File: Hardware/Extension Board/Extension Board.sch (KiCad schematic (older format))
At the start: 34 parts, among them J1 CNX_LED, J10 MODE, J11 TUNING, J12 I2C, J13 I2C, J14 SPI, J15 SD, J16 TFT, J2 CNX_LED, J3 CNX_LED, J4 CNX_LED, J5 SPARE, J6 ARDUINO_DIGITAL, J7 ARDUINO_COMMS, J8 ARDUINO_ANALOG, J9 NEXT_AGAIN, U1 74HC14

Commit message: update shematics
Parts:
- removed J15: SD, Connector_JST:JST_XH_B4B-XH-AM_1x04_P2.50mm_Vertical, symbol Connector_Generic:Conn_01x04
- removed J16: TFT, Connector_JST:JST_XH_B8B-XH-AM_1x08_P2.50mm_Vertical, symbol Connector_Generic:Conn_01x08
- added J15, J5: CNX_LED, Connector_JST:JST_XH_B2B-XH-A_1x02_P2.50mm_Vertical, symbol Connector_Generic:Conn_01x02
- added R11, R12: 200, Resistor_THT:R_Axial_DIN0207_L6.3mm_D2.5mm_P10.16mm_Horizontal, symbol Device:R
- added TP3: TestPoint_Flag, TestPoint:TestPoint_Loop_D2.54mm_Drill1.5mm_Beaded, symbol Connector:TestPoint_Flag
- added U2: LM7806_TO220, Package_TO_SOT_THT:TO-220-3_Vertical, symbol Regulator_Linear:LM7806_TO220
- added U3: LM7812_TO220, Package_TO_SOT_THT:TO-220-3_Vertical, symbol Regulator_Linear:LM7812_TO220
- renumbered J5 to J16
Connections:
- net D17 is gone; now on net SDA: J7.5 (Pin_5)
- net A12: now also J8.5 (Pin_5); no longer J8.4 (Pin_4)
- net A14: now also J8.7 (Pin_7); no longer J8.2 (Pin_2)
- net D18: now also J7.3 (Pin_3); no longer J7.4 (Pin_4)
- net D19: now also J7.4 (Pin_4); no longer J7.3 (Pin_3)
- net GND: no longer TP2.1
- net SCL: now also J7.6 (Pin_6); no longer J7.1 (Pin_1)
- net SDA: no longer J7.2 (Pin_2)
- net VCC: now also J15.1 (Pin_1), J5.1 (Pin_1); no longer TP1.1
- net at J1.2 (Pin_2): now also R11.1; no longer R1.1
- net at J16.2 (Pin_2): now also R12.1; no longer R5.1
- net D35: now reaches J6.15 (Pin_15)
- net D35: now also R11.2
- net D37: now reaches J6.17 (Pin_17)
- net D37: now also R12.2
- net TFT_LED: no longer names the net of R9.1
- net TFT_LED: no longer R10.1
- new net: J15.2 (Pin_2), R1.1
- new net: J5.2 (Pin_2), R5.1
- no-connect marks 25 -> 24
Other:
- note added: "A15 ... ... A8"
- note added: "ALIMENTATION"
- note added: "D21 ... ... D16"
- note removed: "SPI OLED DISPLAY"
- moved on the sheet: J1, J16, TP1, TP2

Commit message: Ajout FootPrint Library MesModules
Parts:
- removed J1, J15, J2, J3, J4, J5: CNX_LED, Connector_JST:JST_XH_B2B-XH-A_1x02_P2.50mm_Vertical, symbol Connector_Generic:Conn_01x02
- removed R4: 200, Resistor_THT:R_Axial_DIN0207_L6.3mm_D2.5mm_P10.16mm_Horizontal, symbol Device:R
- removed R9: 50k, Resistor_THT:R_Axial_DIN0207_L6.3mm_D2.5mm_P10.16mm_Horizontal, symbol Device:R
- added C3: 100uF, Capacitor_THT:CP_Axial_L18.0mm_D8.0mm_P25.00mm_Horizontal, symbol Device:CP
- added C4: 2200uF, Capacitor_THT:CP_Axial_L30.0mm_D18.0mm_P35.00mm_Horizontal, symbol Device:CP
- added C5, C6: 10uF, Capacitor_THT:CP_Radial_D5.0mm_P2.50mm, symbol Device:CP
- added HS1: Heatsink, MesModules:HeatSink_TO-220, symbol Mechanical:Heatsink
- added J10: CNX ON_OFF, Connector_JST:JST_XH_B2B-XH-A_1x02_P2.50mm_Vertical, symbol Connector_Generic:Conn_01x02
- added J13: CNX_LAMPS, MesModules:Bloc_de_jonction_CI-MPT_2.54mm_01x02, symbol Connector:Screw_Terminal_01x02
- added J14: CNX_6V, TerminalBlock_Phoenix:TerminalBlock_Phoenix_MKDS-1,5-2-5.08_1x02_P5.08mm_Horizontal, symbol Connector:Screw_Terminal_01x02
- added J15: CNX_12V, TerminalBlock_Phoenix:TerminalBlock_Phoenix_MKDS-1,5-2-5.08_1x02_P5.08mm_Horizontal, symbol Connector:Screw_Terminal_01x02
- added J6: CNX LEDS, symbol Connector_Generic:Conn_02x05_Odd_Even
- added J9: CNX POWER, TerminalBlock_Phoenix:TerminalBlock_Phoenix_MKDS-1,5-2-5.08_1x02_P5.08mm_Horizontal, symbol Connector:Screw_Terminal_01x02
- added JP1: Jumper, Connector_PinHeader_2.54mm:PinHeader_1x02_P2.54mm_Vertical, symbol Device:Jumper_NC_Small
- added JP2: Jumper, Connector_PinHeader_2.54mm:PinHeader_1x02_P2.54mm_Vertical, symbol Device:Jumper_NO_Small
- added R11: 3k3, Resistor_THT:R_Axial_DIN0207_L6.3mm_D2.5mm_P10.16mm_Horizontal, symbol Device:R
- added TP4: TestPoint 12V, TestPoint:TestPoint_Loop_D2.54mm_Drill1.5mm_Beaded, symbol Connector:TestPoint_Flag
- J11: value TUNING -> CNX TUNE
- J4: renamed from J14; value SPI -> CNX SPI
- J5: renamed from J10; value MODE -> CNX MODE
- J7: renamed from J16; value SPARE -> CNX SPARE; footprint Connector_JST:JST_XH_B3B-XH-A_1x03_P2.50mm_Vertical -> Connector_JST:JST_XH_B3B-XH-AM_1x03_P2.50mm_Vertical
- R10: value 90k -> 3k3
- R7, R8: value 4.7k -> 3k3
- R9: renamed from R6; value A CALCULER -> 3M; footprint Resistor_THT:R_Axial_DIN0411_L9.9mm_D3.6mm_P20.32mm_Horizontal -> (none)
- TP1: value TestPoint_Flag -> TestPoint GND
- TP2: value TestPoint_Flag -> TestPoint VDD
- TP3: value TestPoint_Flag -> TestPoint 6V
- renumbered J6 to J1, J13 to J16, J7 to J2, J8 to J3, J9 to J8, R5 to R1, R11 to R2, R1 to R3, R2 to R4, R3 to R5, R12 to R6
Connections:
- net A12: now also JP1.1, JP2.1; no longer J11.2 (Pin_2)
- net GND: now also TP1.1, U2.2 (GND), U3.2 (GND), C3.2, C4.2, C5.2, C6.2, J13.2 (Pin_2), J14.2 (Pin_2), J15.2 (Pin_2), J9.1 (Pin_1), JP2.2
- net SCL: now also R11.2
- net SDA: now also R10.2
- net VCC: now also R10.1, TP3.1, U2.3 (VO), C5.1, J13.1 (Pin_1), J14.1 (Pin_1), J6.10 (Pin_10), J6.2 (Pin_2), J6.4 (Pin_4), J6.6 (Pin_6), J6.8 (Pin_8), R11.1; no longer R10.2
- net at R5.1: now also J6.9 (Pin_9)
- net at R4.1: now also J6.7 (Pin_7)
- net at R2.1: now also J6.3 (Pin_3)
- net VDD: now reaches TP2.1
- net VDD: now also U2.1 (VI), U3.1 (VI), C3.1, C4.1, J10.2 (Pin_2)
- net at R3.1: now also J6.5 (Pin_5)
- net at R1.1: now also J6.1 (Pin_1)
- net +12V: now reaches U3.3 (VO)
- net +12V: now also C6.1, J15.1 (Pin_1), TP4.1
- new net: J10.1 (Pin_1), J9.2 (Pin_2)
- new net C1: J11.2 (Pin_2), JP1.2
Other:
- note added: "Adaptation pour Push Buttons \n(avec IRQ)"
- note added: "Adaptation pour \nRotary Button"
- note added: "Ampli 7W/12V:\n→600mA"
- note added: "I2C bus"
- note added: "Spare connectors"
- note added: "verifier s'il faut connecter à la masse"
- note removed: "Adaptation pour Push Buttons (avec IRQ)"
- note removed: "Adaptation pour Rotary Button"
- note removed: "SPI and I2C bus"
- moved on the sheet: C1, C2, J11, J12, J16, J2, J4, J5, J7, J8, R1, R2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

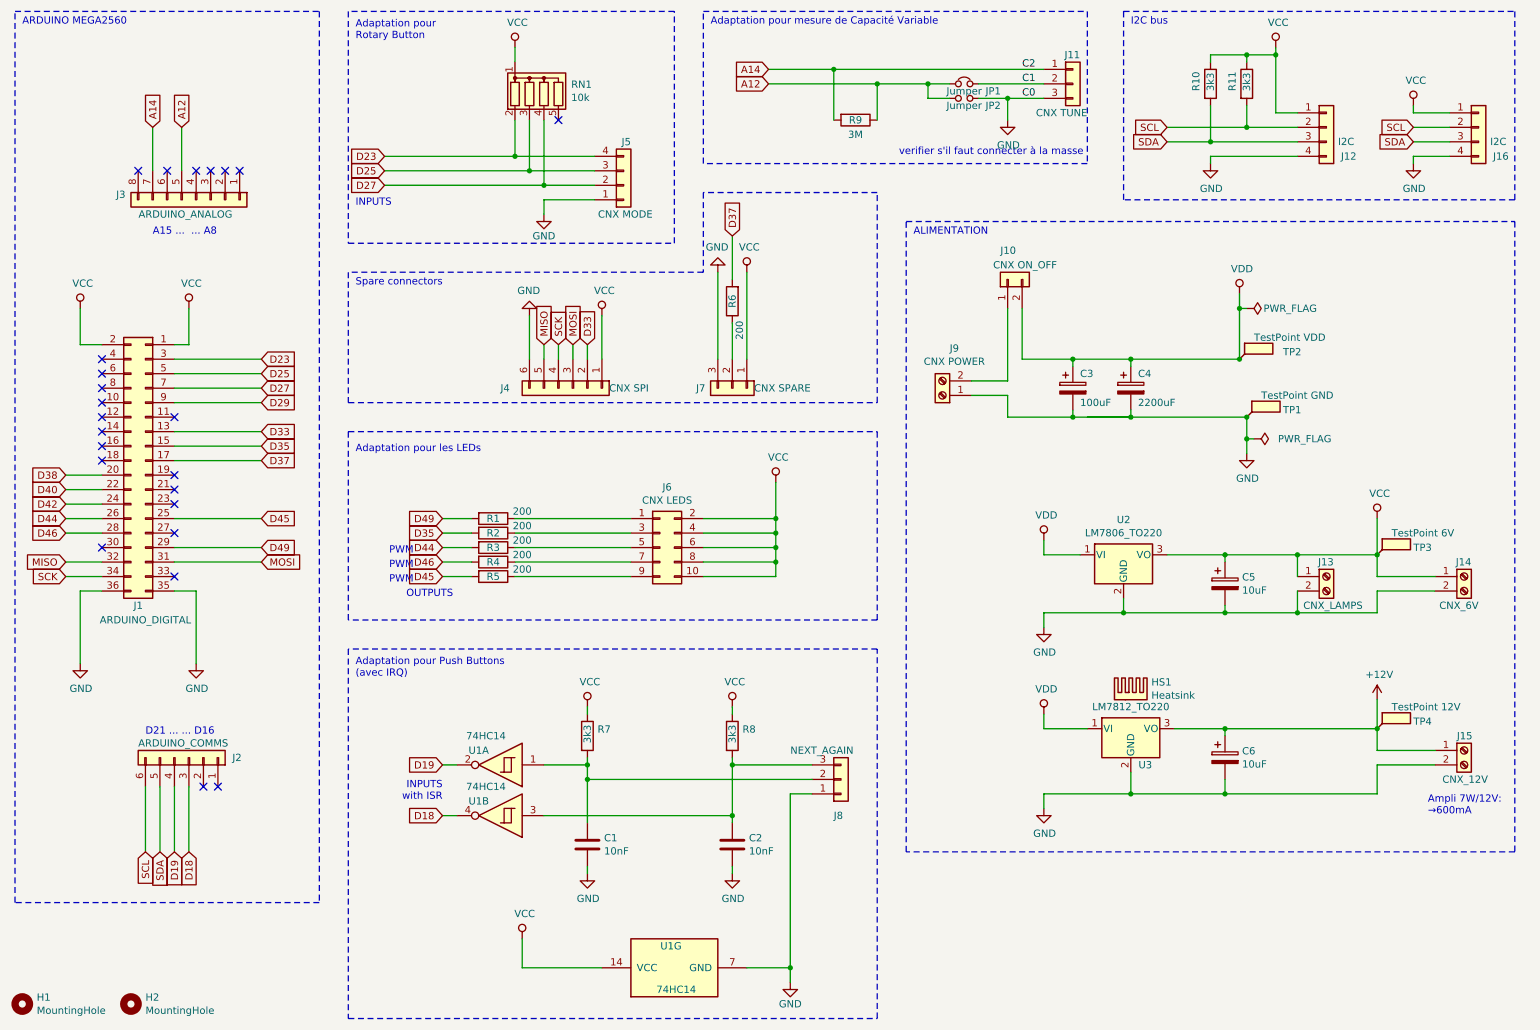
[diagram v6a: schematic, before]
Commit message: Ajout du connecteur HE10 10P dans la Library KiCad
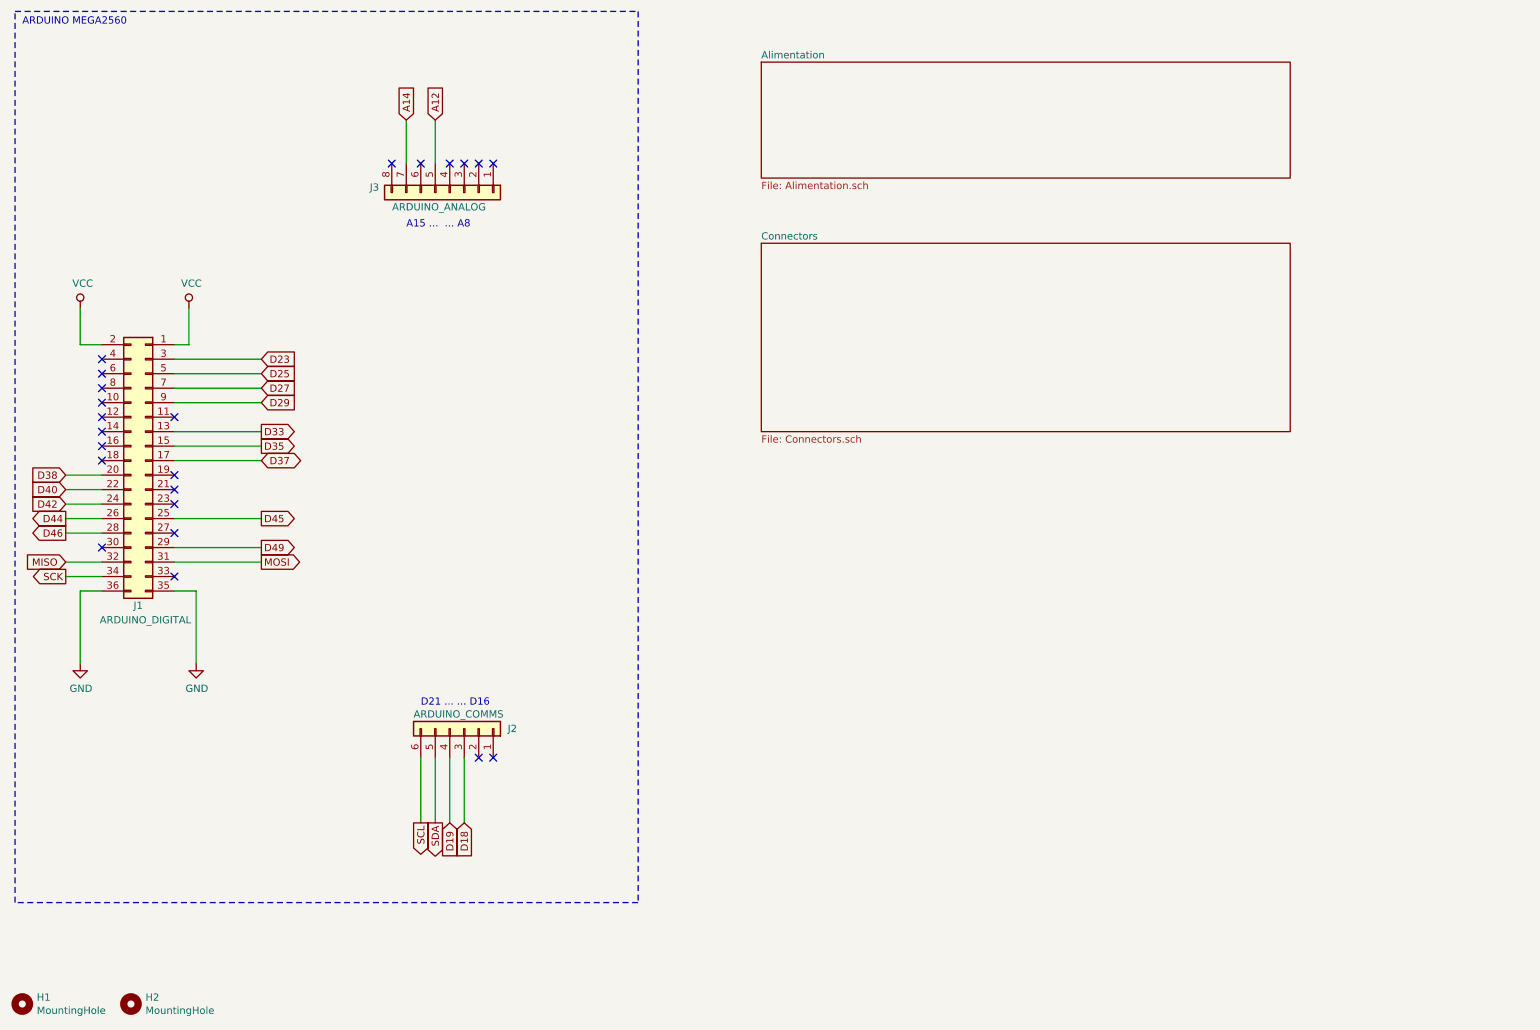
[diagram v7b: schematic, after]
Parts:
- removed C1, C2: 10nF, Capacitor_THT:C_Rect_L7.2mm_W2.5mm_P5.00mm_FKS2_FKP2_MKS2_MKP2, symbol Device:C
- removed C3: 100uF, Capacitor_THT:CP_Axial_L18.0mm_D8.0mm_P25.00mm_Horizontal, symbol Device:CP
- removed C4: 2200uF, Capacitor_THT:CP_Axial_L30.0mm_D18.0mm_P35.00mm_Horizontal, symbol Device:CP
- removed C5, C6: 10uF, Capacitor_THT:CP_Radial_D5.0mm_P2.50mm, symbol Device:CP
- removed HS1: Heatsink, MesModules:HeatSink_TO-220, symbol Mechanical:Heatsink
- removed J10: CNX ON_OFF, Connector_JST:JST_XH_B2B-XH-A_1x02_P2.50mm_Vertical, symbol Connector_Generic:Conn_01x02
- removed J11: CNX TUNE, Connector_JST:JST_XH_B3B-XH-A_1x03_P2.50mm_Vertical, symbol Connector_Generic:Conn_01x03
- removed J12, J16: I2C, Connector_JST:JST_XH_B4B-XH-A_1x04_P2.50mm_Vertical, symbol Connector_Generic:Conn_01x04
- removed J13: CNX_LAMPS, MesModules:Bloc_de_jonction_CI-MPT_2.54mm_01x02, symbol Connector:Screw_Terminal_01x02
- removed J14: CNX_6V, TerminalBlock_Phoenix:TerminalBlock_Phoenix_MKDS-1,5-2-5.08_1x02_P5.08mm_Horizontal, symbol Connector:Screw_Terminal_01x02
- removed J15: CNX_12V, TerminalBlock_Phoenix:TerminalBlock_Phoenix_MKDS-1,5-2-5.08_1x02_P5.08mm_Horizontal, symbol Connector:Screw_Terminal_01x02
- removed J4: CNX SPI, Connector_JST:JST_XH_B6B-XH-AM_1x06_P2.50mm_Vertical, symbol Connector_Generic:Conn_01x06
- removed J5: CNX MODE, Connector_JST:JST_XH_B4B-XH-A_1x04_P2.50mm_Vertical, symbol Connector_Generic:Conn_01x04
- removed J6: CNX LEDS, symbol Connector_Generic:Conn_02x05_Odd_Even
- removed J7: CNX SPARE, Connector_JST:JST_XH_B3B-XH-AM_1x03_P2.50mm_Vertical, symbol Connector_Generic:Conn_01x03
- removed J8: NEXT_AGAIN, Connector_JST:JST_XH_B3B-XH-A_1x03_P2.50mm_Vertical, symbol Connector_Generic:Conn_01x03
- removed J9: CNX POWER, TerminalBlock_Phoenix:TerminalBlock_Phoenix_MKDS-1,5-2-5.08_1x02_P5.08mm_Horizontal, symbol Connector:Screw_Terminal_01x02
- removed JP1: Jumper, Connector_PinHeader_2.54mm:PinHeader_1x02_P2.54mm_Vertical, symbol Device:Jumper_NC_Small
- removed JP2: Jumper, Connector_PinHeader_2.54mm:PinHeader_1x02_P2.54mm_Vertical, symbol Device:Jumper_NO_Small
- removed R1, R2, R3, R4, R5, R6: 200, Resistor_THT:R_Axial_DIN0207_L6.3mm_D2.5mm_P10.16mm_Horizontal, symbol Device:R
- removed R10, R11, R7, R8: 3k3, Resistor_THT:R_Axial_DIN0207_L6.3mm_D2.5mm_P10.16mm_Horizontal, symbol Device:R
- removed R9: 3M, symbol Device:R
- removed RN1: 10k, Resistor_THT:R_Array_SIP5, symbol Device:R_Network04
- removed TP1: TestPoint GND, TestPoint:TestPoint_Loop_D2.54mm_Drill1.5mm_Beaded, symbol Connector:TestPoint_Flag
- removed TP2: TestPoint VDD, TestPoint:TestPoint_Loop_D2.54mm_Drill1.5mm_Beaded, symbol Connector:TestPoint_Flag
- removed TP3: TestPoint 6V, TestPoint:TestPoint_Loop_D2.54mm_Drill1.5mm_Beaded, symbol Connector:TestPoint_Flag
- removed TP4: TestPoint 12V, TestPoint:TestPoint_Loop_D2.54mm_Drill1.5mm_Beaded, symbol Connector:TestPoint_Flag
- removed U1: 74HC14, Package_DIP:DIP-14_W7.62mm_Socket_LongPads, symbol 74xx:74HC14
- removed U2: LM7806_TO220, Package_TO_SOT_THT:TO-220-3_Vertical, symbol Regulator_Linear:LM7806_TO220
- removed U3: LM7812_TO220, Package_TO_SOT_THT:TO-220-3_Vertical, symbol Regulator_Linear:LM7812_TO220
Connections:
- no-connect marks 24 -> 23
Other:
- note removed: "ALIMENTATION"
- note removed: "Adaptation pour Push Buttons \n(avec IRQ)"
- note removed: "Adaptation pour \nRotary Button"
- note removed: "Adaptation pour les LEDs"
- note removed: "Adaptation pour mesure de Capacité Variable"
- note removed: "Ampli 7W/12V:\n→600mA"
- note removed: "I2C bus"
- note removed: "INPUTS"
- note removed: "INPUTS\nwith ISR"
- note removed: "OUTPUTS"
- note removed: "PWM"
- note removed: "Spare connectors"
- note removed: "verifier s'il faut connecter à la masse"
- moved on the sheet: J2, J3
